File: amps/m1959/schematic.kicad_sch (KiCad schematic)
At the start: 95 parts, among them T1 OT

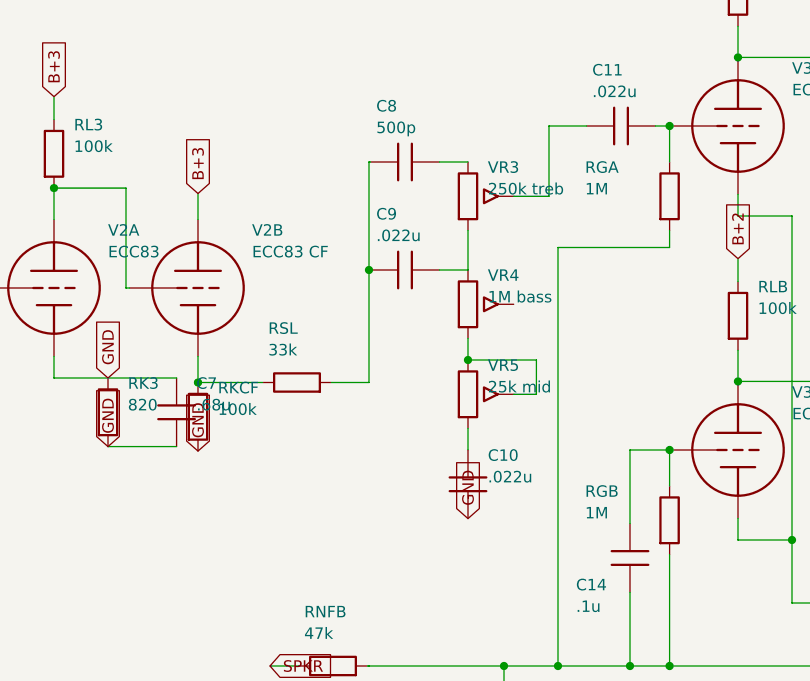
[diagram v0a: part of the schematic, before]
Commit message: Fix: the drawn tone stacks now are the tone stack the lab plots, and a gate says so
The tone-stack lab solves one network — the FMV stack documented in
site/src/lib/tonestack.js — and fills its values from each amp's BOM by
reference designator. Nothing checked that the schematic drew those
designators into that network, and nine of the nine drawings did not.

What the drawings said, rebuilt from the committed .kicad_sch files rather
than from the generators:

- 5F6-A, JTM45, 1987, 1959 and 5F4 ran the treble capacitor off the slope
  resistor's FOOT instead of the stack input, and landed the treble pot's
  lower lug on the bass-capacitor node instead of the slope foot.
- Every three-knob drawing left the bass pot's wiper unwired, so the plotted
  output (treble wiper AND bass wiper) existed on no drawing.
- JTM45, 1987 and 1959 put the mid capacitor in series with the mid pot down
  to ground rather than from the slope foot to the mid leg's top.
- 5F6 tied its bass pot as a rheostat and fed the mid capacitor to the middle
  pot's wiper.
- The blackface circuits left the treble pot's lower lug on the bass-cap node
  and tied the bass wiper to its own lug; AB763 drew its 0.047 µF inline on
  top of the bass pot's lug.

The 5F6-A's own layout.yaml — redrawn from the published Fender 5F6-A layout
sheet — already wires the canonical network (treble low to the slope node,
both wipers to the phase-inverter coupler), and 5F4's does too, so the
drawings were corrected to that rather than the lab to the drawings.

Consequences beyond the wires:

- 5F6-A's parts list prints one 0.02 µF line covering the bass and middle
  positions; the drawing showed one capacitor where the circuit has two.
  Added C5b with the same value and the same printed line cited. The plotted
  curve does not move — both positions already used that value.
- The blackface stacks keep the capacitor that feeds the mid leg. With the
  lug corrected, CBN/CB1 (0.1 µF) feeds the bass pot and CBN2/CB2 (0.047 µ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
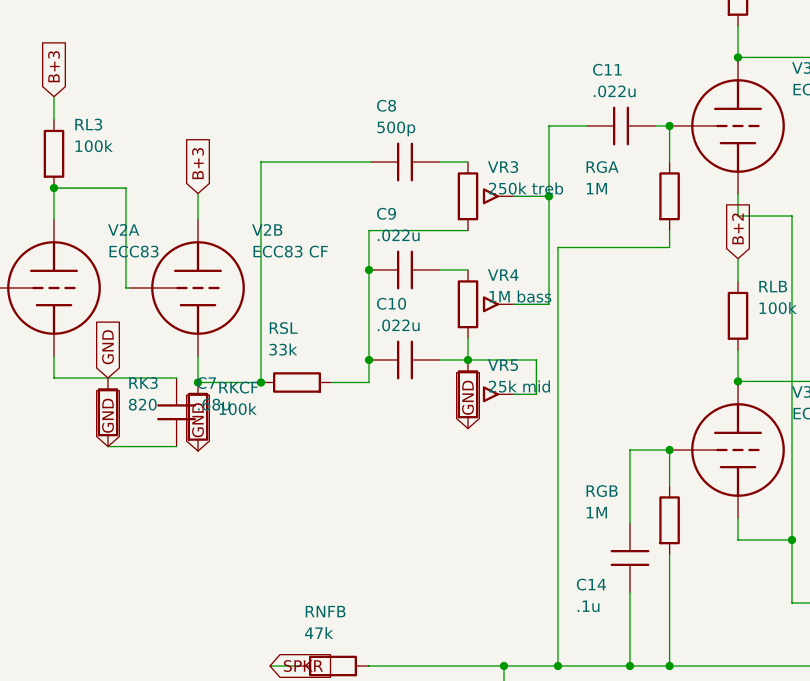
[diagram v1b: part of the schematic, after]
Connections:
- net GND: now also VR5.3; no longer C10.2
- net at C9.2, VR4.1: no longer VR3.3
- net at VR4.2 (W): now also C11.1, VR3.2 (W)
- net at VR4.3, VR5.1, VR5.2 (W): now also C10.2
- net at RKCF.1, RSL.1, V2B.3 (K): now also C8.1
- net at C9.1, RSL.2: now also C10.1, VR3.3; no longer C8.1
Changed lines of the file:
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@@
   (wire (pts (xy 133 150.5) (xy 133.19 150.5))
+    (stroke (width 0) (type default)))
+  (junction (at 133 150.5) (diameter 0) (color 0 0 0 0))
+  (wire (pts (xy 133 150.5) (xy 133 126))
     (stroke (width 0) (type default)))
   (wire (pts (xy 140.81 150.5) (xy 145 150.5))
     (stroke (width 0) (type default)))
-  (wire (pts (xy 145 150.5) (xy 145 126))
+  (wire (pts (xy 145 150.5) (xy 145 133.62))
+    (stroke (width 0) (type default)))
+  (wire (pts (xy 145 133.62) (xy 156 133.62))
     (stroke (width 0) (type default)))
   (junction (at 145 138) (diameter 0) (color 0 0 0 0))
+  (junction (at 145 148) (diameter 0) (color 0 0 0 0))
   (symbol (lib_id "cx:C") (at 149 126 90) (unit 1)
     (in_bom yes) (on_board yes)
     (property "Reference" "C8" (at 145.8 119.8 270) (effects (font (size 1.27 1.27)) (justify left)))
     (property "Value" "500p" (at 145.8 122.2 270) (effects (font (size 1.27 1.27)) (justify left))))
-  (wire (pts (xy 145 126) (xy 145.19 126))
+  (wire (pts (xy 133 126) (xy 145.19 126))
     (stroke (width 0) (type default)))
   (wire (pts (xy 152.81 126) (xy 156 126))
@@
   (wire (pts (xy 152.81 138) (xy 156 138))
     (stroke (width 0) (type default)))
-  (wire (pts (xy 156 133.62) (xy 156 138))
-    (stroke (width 0) (type default)))
   (symbol (lib_id "cx:POT") (at 156 141.81 0) (unit 1)
     (in_bom yes) (on_board yes)
     (property "Reference" "VR4" (at 158.2 138.61 0) (effects (font (size 1.27 1.27)) (justify left)))
     (property "Value" "1M bass" (at 158.2 141.01 0) (effects (font (size 1.27 1.27)) (justify left))))
+  (symbol (lib_id "cx:C") (at 149 148 90) (unit 1)
+    (in_bom yes) (on_board yes)
+    (property "Reference" "C10" (at 145.8 141.8 270) (effects (font (size 1.27 1.27)) (justify left)))
+    (property "Value" ".022u" (at 145.8 144.2 270) (effects (font (size 1.27 1.27)) (justify left))))
+  (wire (pts (xy 145 148) (xy 145.19 148))
+    (stroke (width 0) (type default)))
+  (wire (pts (xy 152.81 148) (xy 156 148))
+    (stroke (width 0) (type default)))
   (wire (pts (xy 156 145.62) (xy 156 148))
     (stroke (width 0) (type default)))
@@
     (property "Reference" "VR5" (at 158.2 148.61 0) (effects (font (size 1.27 1.27)) (justify left)))
     (property "Value" "25k mid" (at 158.2 151.01 0) (effects (font (size 1.27 1.27)) (justify left))))
-  (wire (pts (xy 156 155.62) (xy 156 158))
-    (stroke (width 0) (type default)))
-  (symbol (lib_id "cx:C") (at 156 161.81 0) (unit 1)
-    (in_bom yes) (on_board yes)
-    (property "Reference" "C10" (at 158.2 158.61 0) (effects (font (size 1.27 1.27)) (justify left)))
-    (property "Value" ".022u" (at 158.2 161.01 0) (effects (font (size 1.27 1.27)) (justify left))))
-  (global_label "GND" (shape input) (at 156 165.62 270)
+  (global_label "GND" (shape input) (at 156 155.62 270)
     (effects (font (size 1.27 1.27)) (justify left)))
   (wire (pts (xy 161.08 151.81) (xy 163.6 151.81))
@@
   (wire (pts (xy 161.08 129.81) (xy 165 129.81))
     (stroke (width 0) (type default)))
+  (wire (pts (xy 161.08 141.81) (xy 165 141.81))
+    (stroke (width 0) (type default)))
+  (wire (pts (xy 165 141.81) (xy 165 129.81))
+    (stroke (width 0) (type default)))
+  (junction (at 165 129.81) (diameter 0) (color 0 0 0 0))
   (wire (pts (xy 165 129.81) (xy 165 122))
     (stroke (width 0) (type default)))

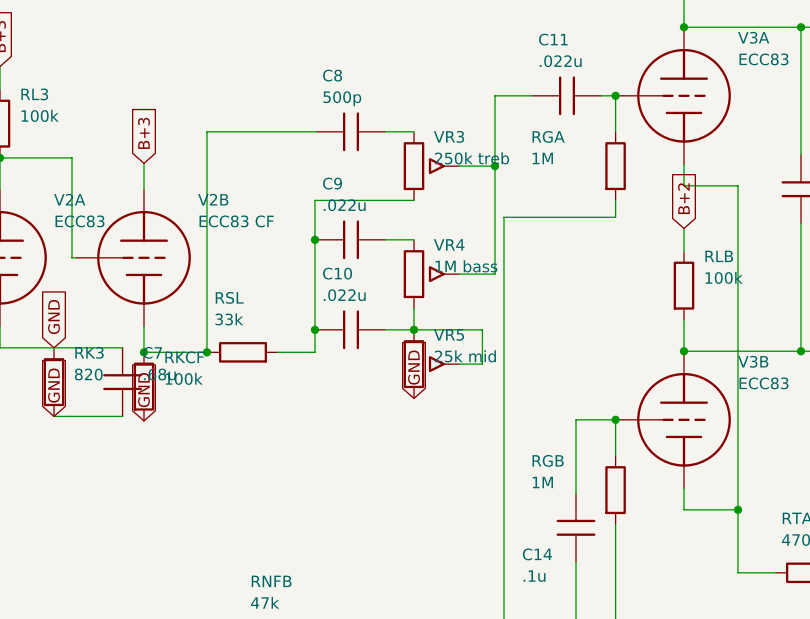
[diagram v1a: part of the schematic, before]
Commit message: Fix: the published sheets draw a different tone stack, and now we draw theirs
The tone-stack pass rewired nine schematics to one "canonical FMV" network —
treble lower lug on the slope foot, treble and bass wipers joined at the
output, mid cap on a rheostat-wired mid pot — on the strength of the 5F6-A
layout.yaml, a redraw that omits the tone capacitors "for legibility" and
whose stack runs were convention, not sheet reading. Fetching the published
drawings and reading them settles what they actually draw, and it is not that
network. Five sheets were read at 300-400 dpi:

- Fender 5F6 (F-EG), schematic AND factory layout pages
- Fender 5F6-A (I-EG), schematic and layout, side by side
- Marshall JTM45 trem ('types 1961, 1962, 1987/T'), Unicord 70-19-11 (1987),
  and the 100 W Type #2 c.1967 (1959)
- Fender Princeton AA964, schematic and factory layout

All of them agree on a ladder: the treble cap and the slope resistor both
leave the stack input; the first bass cap lands on the node shared by the
treble pot's LOWER lug and the bass pot — the treble pot's cold end sits on
the far side of that capacitor, not on the slope foot; the bass pot is a
rheostat (arrow-through-body on most sheets; the JTM45 loops its wiper to the
foot lug, the 5F6 factory layout straps it into the treble-lug node) in
series down the ladder; the mid cap feeds the MIDDLE POT'S WIPER, not its
top; and the stack's output is the treble wiper ALONE. The blackface AA964
draws the same ladder with its 6.8k fixed leg. The 5F6's presence-in-the-
ground-leg arrangement is unchanged and was always right.

So five drawings return to their sheets: 5f6 and aa964 revert to their
pre-rewire wiring (which the extractor confirms matched the sheets all
along), and jtm45/m1987/m1959 are redrawn to the sheets outright — their old
drawings were wrong differently (treble cap off the slope foot, mid cap in
series to ground, bass wiper floating), so neither old nor "canonical" would
do.

The lab keeps all five as prese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
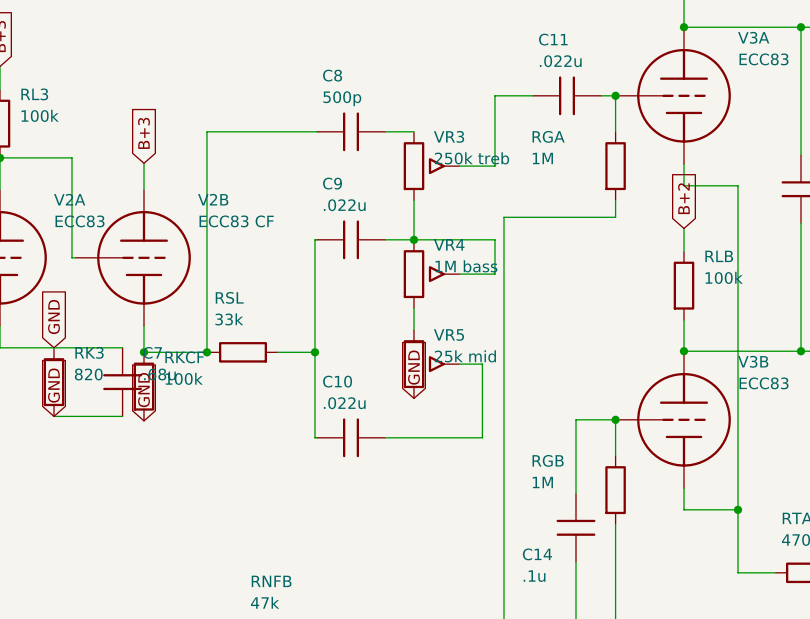
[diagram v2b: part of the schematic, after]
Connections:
- net at C11.1, VR3.2 (W): no longer VR4.2 (W)
- net at C10.1, C9.1, RSL.2: no longer VR3.3
- net at C9.2, VR4.1: now also VR3.3, VR4.2 (W)
- net at VR4.3, VR5.1: no longer C10.2, VR5.2 (W)
- new net: C10.2, VR5.2 (W)
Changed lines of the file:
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@@
   (wire (pts (xy 140.81 150.5) (xy 145 150.5))
     (stroke (width 0) (type default)))
-  (wire (pts (xy 145 150.5) (xy 145 133.62))
+  (junction (at 145 150.5) (diameter 0) (color 0 0 0 0))
+  (wire (pts (xy 145 150.5) (xy 145 138))
     (stroke (width 0) (type default)))
-  (wire (pts (xy 145 133.62) (xy 156 133.62))
+  (wire (pts (xy 145 150.5) (xy 145 160))
     (stroke (width 0) (type default)))
-  (junction (at 145 138) (diameter 0) (color 0 0 0 0))
-  (junction (at 145 148) (diameter 0) (color 0 0 0 0))
   (symbol (lib_id "cx:C") (at 149 126 90) (unit 1)
     (in_bom yes) (on_board yes)
@@
   (wire (pts (xy 152.81 138) (xy 156 138))
     (stroke (width 0) (type default)))
+  (wire (pts (xy 156 133.62) (xy 156 138))
+    (stroke (width 0) (type default)))
+  (junction (at 156 138) (diameter 0) (color 0 0 0 0))
   (symbol (lib_id "cx:POT") (at 156 141.81 0) (unit 1)
     (in_bom yes) (on_board yes)
     (property "Reference" "VR4" (at 158.2 138.61 0) (effects (font (size 1.27 1.27)) (justify left)))
     (property "Value" "1M bass" (at 158.2 141.01 0) (effects (font (size 1.27 1.27)) (justify left))))
-  (symbol (lib_id "cx:C") (at 149 148 90) (unit 1)
+  (wire (pts (xy 161.08 141.81) (xy 165 141.81))
+    (stroke (width 0) (type default)))
+  (wire (pts (xy 165 141.81) (xy 165 138))
+    (stroke (width 0) (type default)))
+  (wire (pts (xy 165 138) (xy 156 138))
+    (stroke (width 0) (type default)))
+  (symbol (lib_id "cx:C") (at 149 160 90) (unit 1)
     (in_bom yes) (on_board yes)
-    (property "Reference" "C10" (at 145.8 141.8 270) (effects (font (size 1.27 1.27)) (justify left)))
-    (property "Value" ".022u" (at 145.8 144.2 270) (effects (font (size 1.27 1.27)) (justify left))))
-  (wire (pts (xy 145 148) (xy 145.19 148))
+    (property "Reference" "C10" (at 145.8 153.8 270) (effects (font (size 1.27 1.27)) (justify left)))
+    (property "Value" ".022u" (at 145.8 156.2 270) (effects (font (size 1.27 1.27)) (justify left))))
+  (wire (pts (xy 145 160) (xy 145.19 160))
     (stroke (width 0) (type default)))
-  (wire (pts (xy 152.81 148) (xy 156 148))
+  (wire (pts (xy 152.81 160) (xy 163.6 160))
+    (stroke (width 0) (type default)))
+  (wire (pts (xy 163.6 160) (xy 163.6 151.81))
+    (stroke (width 0) (type default)))
+  (wire (pts (xy 163.6 151.81) (xy 161.08 151.81))
     (stroke (width 0) (type default)))
   (wire (pts (xy 156 145.62) (xy 156 148))
@@
   (global_label "GND" (shape input) (at 156 155.62 270)
     (effects (font (size 1.27 1.27)) (justify left)))
-  (wire (pts (xy 161.08 151.81) (xy 163.6 151.81))
-    (stroke (width 0) (type default)))
-  (wire (pts (xy 163.6 151.81) (xy 163.6 148))
-    (stroke (width 0) (type default)))
-  (wire (pts (xy 163.6 148) (xy 156 148))
-    (stroke (width 0) (type default)))
-  (junction (at 156 148) (diameter 0) (color 0 0 0 0))
   (wire (pts (xy 161.08 129.81) (xy 165 129.81))
     (stroke (width 0) (type default)))
-  (wire (pts (xy 161.08 141.81) (xy 165 141.81))
-    (stroke (width 0) (type default)))
-  (wire (pts (xy 165 141.81) (xy 165 129.81))
-    (stroke (width 0) (type default)))
-  (junction (at 165 129.81) (diameter 0) (color 0 0 0 0))
   (wire (pts (xy 165 129.81) (xy 165 122))
     (stroke (width 0) (type default)))
